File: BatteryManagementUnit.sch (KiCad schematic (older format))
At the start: 12 parts

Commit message: triac hack
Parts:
- removed U?: OPTO-TRANSISTOR, symbol OPTO-TRANSISTOR
- added Q?: Q_NPN_BCE, symbol Q_NPN_BCE
- added U?: OPTO-TRIAC, symbol OPTO-TRIAC
- P1: renamed from P?; footprint (none) -> Pin_Headers:Pin_Header_Angled_1x04
- P2, P3: renamed from P?; footprint (none) -> Pin_Headers:Pin_Header_Angled_1x02
- P4, P5: renamed from P?; footprint (none) -> Connect:bornier2
- Q1, Q2: renamed from Q?; footprint (none) -> TO_SOT_Packages_SMD:TO-252-2Lead
- R1, R2: renamed from R?; footprint (none) -> Resistors_SMD:R_1210_HandSoldering
- U2: renamed from U?; footprint (none) -> electric_car_lib:amc1301
- gave numbers to parts that had none: 1
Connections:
- wire segments 38 -> 39
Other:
- note removed: "CHOOSE HIGH VOLTAGE OPTO TRANSISTOR"

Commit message: partial layout
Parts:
- added P104: CONT_H_mon, Connect:bornier2, symbol CONN_01X02
- added P105: CONT_L_mon, Connect:bornier2, symbol CONN_01X02
- added P?: Battery, Connect:bornier2, symbol CONN_01X02
- Q101: renamed from Q?; footprint (none) -> TO_SOT_Packages_SMD:SOT-23_Handsoldering
- gave numbers to parts that had none: 1
- renumbered P1 to P101, P2 to P102, P3 to P103, P4 to P106, P5 to P107, Q1 to Q102, Q2 to Q103, R1 to R101, R2 to R102, U2 to U102, U3 to U103
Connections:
- wire segments 39 -> 47
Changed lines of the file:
@@
 $Descr A4 11693 8268
 encoding utf-8
-Sheet 1 1
+Sheet 1 2
 Title ""
 Date ""
@@
 $EndDescr
 $Comp
-L CONN_01X04 P1
+L CONN_01X04 P101
 U 1 1 57FC851F
 P 2800 1300
-F 0 "P1" H 2800 1550 50  0000 C CNN
+F 0 "P101" H 2800 1550 50  0000 C CNN
 F 1 "HALL EFFECT" V 2900 1300 50  0000 C CNN
 F 2 "Pin_Headers:Pin_Header_Angled_1x04" H 2800 1300 50  0001 C CNN
@@
 $EndComp
 $Comp
-L AMC1301 U2
+L AMC1301 U102
 U 1 1 57FC8658
 P 2400 6650
-F 0 "U2" H 2400 6300 60  0000 C CNN
+F 0 "U102" H 2400 6300 60  0000 C CNN
 F 1 "AMC1301" H 2400 7000 60  0000 C CNN
 F 2 "electric_car_lib:amc1301" H 2450 6200 60  0001 C CNN
@@
 $EndComp
 $Comp
-L R R1
+L R R101
 U 1 1 57FC8843
 P 1050 5200
-F 0 "R1" V 1130 5200 50  0000 C CNN
+F 0 "R101" V 1130 5200 50  0000 C CNN
 F 1 "R" V 1050 5200 50  0000 C CNN
 F 2 "Resistors_SMD:R_1210_HandSoldering" V 980 5200 50  0001 C CNN
@@
 $EndComp
 $Comp
-L R R2
+L R R102
 U 1 1 57FC8882
 P 1050 6050
-F 0 "R2" V 1130 6050 50  0000 C CNN
+F 0 "R102" V 1130 6050 50  0000 C CNN
 F 1 "R" V 1050 6050 50  0000 C CNN
 F 2 "Resistors_SMD:R_1210_HandSoldering" V 980 6050 50  0001 C CNN
@@
 $EndComp
 $Comp
-L Q_NMOS_DGS Q1
+L Q_NMOS_DGS Q102
 U 1 1 57FCE6EE
 P 8700 1550
-F 0 "Q1" H 9000 1600 50  0000 R CNN
+F 0 "Q102" H 9000 1600 50  0000 R CNN
 F 1 "Q_NMOS_DGS" H 9350 1500 50  0000 R CNN
 F 2 "TO_SOT_Packages_SMD:TO-252-2Lead" H 8900 1650 50  0001 C CNN
@@
 $EndComp
 $Comp
-L Teensy_3.2 U3
+L Teensy_3.2 U103
 U 1 1 57FCF1AF
 P 9500 4700
-F 0 "U3" H 9500 4550 39  0000 C CNN
+F 0 "U103" H 9500 4550 39  0000 C CNN
 F 1 "Teensy_3.2" H 9500 5250 39  0000 C CNN
 F 2 "" H 9200 4250 39  0001 C CNN
@@
 	1    0    0    -1
 $EndComp
-Text Label 1550 4500 1    60   ~ 0
+Text Label 850  4600 1    60   ~ 0
 HV+
 Text Label 1000 6650 1    60   ~ 0
@@
 out
 $Comp
-L CONN_01X02 P4
+L CONN_01X02 P106
 U 1 1 57FD399B
 P 8650 950
-F 0 "P4" H 8650 1100 50  0000 C CNN
+F 0 "P106" H 8650 1100 50  0000 C CNN
 F 1 "CONT_H" V 8750 950 50  0000 C CNN
 F 2 "Connect:bornier2" H 8650 950 50  0001 C CNN
@@
 CNT_H
 $Comp
-L Q_NMOS_DGS Q2
+L Q_NMOS_DGS Q103
 U 1 1 57FD434A
 P 10000 1550
-F 0 "Q2" H 10300 1600 50  0000 R CNN
+F 0 "Q103" H 10300 1600 50  0000 R CNN
 F 1 "Q_NMOS_DGS" H 10650 1500 50  0000 R CNN
 F 2 "TO_SOT_Packages_SMD:TO-252-2Lead" H 10200 1650 50  0001 C CNN
@@
 $EndComp
 $Comp
-L CONN_01X02 P5
+L CONN_01X02 P107
 U 1 1 57FD4357
 P 9950 950
-F 0 "P5" H 9950 1100 50  0000 C CNN
+F 0 "P107" H 9950 1100 50  0000 C CNN
 F 1 "CONT_L" V 10050 950 50  0000 C CNN
 F 2 "Connect:bornier2" H 9950 950 50  0001 C CNN
@@
 cell monitor
 $Comp
-L CONN_01X02 P3
+L CONN_01X02 P103
 U 1 1 57FD4B7A
 P 5350 4150
-F 0 "P3" H 5350 4300 50  0000 C CNN
+F 0 "P103" H 5350 4300 50  0000 C CNN
 F 1 "CONN_01X02" V 5450 4150 50  0000 C CNN
 F 2 "Pin_Headers:Pin_Header_Angled_1x02" H 5350 4150 50  0001 C CNN
@@
 $EndComp
 $Comp
-L CONN_01X02 P2
+L CONN_01X02 P102
 U 1 1 57FD4C12
 P 5300 5000
-F 0 "P2" H 5300 5150 50  0000 C CNN
+F 0 "P102" H 5300 5150 50  0000 C CNN
 F 1 "CONN_01X02" V 5400 5000 50  0000 C CNN
 F 2 "Pin_Headers:Pin_Header_Angled_1x02" H 5300 5000 50  0001 C CNN
@@
 c_m_L
 $Comp
-L OPTO-TRIAC U?
+L OPTO-TRIAC U101
 U 1 1 580F364D
 P 2200 4550
-F 0 "U?" H 2000 4750 50  0000 L CNN
+F 0 "U101" H 2000 4750 50  0000 L CNN
 F 1 "OPTO-TRIAC" H 2000 4350 50  0000 L CNN
-F 2 "" H 2200 4550 50  0000 L CIN
+F 2 "" H 2200 4550 50  0001 L CIN
 F 3 "" H 2175 4550 50  0000 L CNN
 	1    2200 4550
@@
 $EndComp
 $Comp
-L Q_NPN_BCE Q?
+L Q_NPN_BCE Q101
 U 1 1 580F386C
 P 1700 4650
-F 0 "Q?" H 2000 4700 50  0000 R CNN
+F 0 "Q101" H 2000 4700 50  0000 R CNN
 F 1 "Q_NPN_BCE" H 2300 4600 50  0000 R CNN
-F 2 "" H 1900 4750 50  0000 C CNN
+F 2 "TO_SOT_Packages_SMD:SOT-23_Handsoldering" H 1900 4750 50  0001 C CNN
 F 3 "" H 1700 4650 50  0000 C CNN
 	1    1700 4650
@@
 Connection ~ 550  4100
 Wire Wire Line
-	1050 5350 1050 5900
+	1050 5350 1050 5600
+Wire Wire Line
+	1050 5600 1050 5900
 Wire Wire Line
 	1050 6200 1050 6800
@@
 Connection ~ 1050 5600
 Wire Wire Line
+	850  6800 1050 6800
+Wire Wire Line
 	1050 6800 1800 6800
 Wire Wire Line
@@
 	4500 3200 7600 3200
 Wire Notes Line
-	7600 3200 7600 6200
+	6550 3200 6550 6200
 Wire Wire Line
 	5550 4100 6150 4100
@@
 	8800 4700 8350 4700
 Wire Wire Line
-	1900 4450 1600 4450
+	850  4450 1600 4450
+Wire Wire Line
+	1600 4450 1900 4450
 Wire Wire Line
 	1600 4850 1050 4850
 Wire Wire Line
-	1050 4800 1050 5050
-Connection ~ 1050 4800
+	1050 4850 1050 4850
+Wire Wire Line
+	1050 4850 1050 5050
+$Comp
+L CONN_01X02 P104
+U 1 1 582A7B5F
+P 5550 1000
+F 0 "P104" H 5550 1150 50  0000 C CNN
+F 1 "CONT_H_mon" V 5650 1000 50  0000 C CNN
+F 2 "Connect:bornier2" H 5550 1000 50  0001 C CNN
+F 3 "" H 5550 1000 50  0000 C CNN
+	1    5550 1000
+	0    -1   -1   0
+$EndComp
+$Comp
+L CONN_01X02 P105
+U 1 1 582A7BD5
+P 6150 1000
+F 0 "P105" H 6150 1150 50  0000 C CNN
+F 1 "CONT_L_mon" V 6250 1000 50  0000 C CNN
+F 2 "Connect:bornier2" H 6150 1000 50  0001 C CNN
+F 3 "" H 6150 1000 50  0000 C CNN
+	1    6150 1000
+	0    -1   -1   0
+$EndComp
+$Sheet
+S 6850 4100 1100 1000
+U 582A80B4
+F0 "CANmodule" 60
+F1 "CANmodule.sch" 60
+F2 "CAN_TX" I R 7950 4400 60
+F3 "CAN_RX" I R 7950 4500 60
+$EndSheet
+Wire Wire Line
+	8800 4400 7950 4400
+Wire Wire Line
+	7950 4500 8800 4500
+$Comp
+L CONN_01X02 P?
+U 1 1 582AAD74
+P 650 4700
+F 0 "P?" H 650 4850 50  0000 C CNN
+F 1 "Battery" V 750 4700 50  0000 C CNN
+F 2 "Connect:bornier2" H 650 4700 50  0001 C CNN
+F 3 "" H 650 4700 50  0000 C CNN
+	1    650  4700
+	-1   0    0    -1
+$EndComp
+Wire Wire Line
+	850  4650 850  4450
+Connection ~ 1600 4450
+Wire Wire Line
+	850  4750 850  6800
+Connection ~ 1050 6800
+Text Label 850  5050 1    60   ~ 0
+HV-
 $EndSCHEMATC

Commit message: completed schematic
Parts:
- added J101: 0, Resistors_SMD:R_1210_HandSoldering, symbol R
- added P109: PSU_ISO_3v, Pin_Headers:Pin_Header_Straight_1x04, symbol CONN_01X04
- added P110: PSU_ISO_5v, Pin_Headers:Pin_Header_Straight_1x04, symbol CONN_01X04
- added Q104, Q105: Q_NPN_BCE, TO_SOT_Packages_SMD:SOT-23_Handsoldering, symbol Q_NPN_BCE
- added R103, R104, R108, R109: 1k, Resistors_SMD:R_1210_HandSoldering, symbol R
- added R105: 10k 2W, Resistors_ThroughHole:Resistor_Cement_KOA-BGR-3N, symbol R
- added R106, R107, R111: 120, Resistors_SMD:R_1210_HandSoldering, symbol R
- added R110: 10K 2W, Resistors_ThroughHole:Resistor_Cement_KOA-BGR-3N, symbol R
- added R112, R113: 33, Resistors_SMD:R_1210_HandSoldering, symbol R
- added U104, U108: TLP2361, electric_car_lib:soic-5, symbol TLP2361
- added U105, U109: OPTO-TRIAC, symbol OPTO-TRIAC
- added U106: AP1117D33, TO_SOT_Packages_SMD:TO-263-3Lead, symbol AP1117D33
- added U107: AP1117E50, TO_SOT_Packages_SMD:TO-263-3Lead, symbol AP1117E50
- P101: footprint Pin_Headers:Pin_Header_Angled_1x04 -> Pin_Headers:Pin_Header_Straight_1x04
- P102: value CONN_01X02 -> cellsL; footprint Pin_Headers:Pin_Header_Angled_1x02 -> Pin_Headers:Pin_Header_Straight_1x02
- P103: value CONN_01X02 -> cellsH; footprint Pin_Headers:Pin_Header_Angled_1x02 -> Pin_Headers:Pin_Header_Straight_1x02
- U103: footprint (none) -> electric_car_lib:Teensy3.2_inv
- gave numbers to parts that had none: 1
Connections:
- net labels added: +3V3, +5VA, 5v_Traction, Cont_rdy_H, Cont_rdy_L, GND, GNDA, GND_Traction, PrechargeH, PrechargeL
- net labels removed: c_m_H, c_m_L, ground, voltage5v
- wire segments 47 -> 117
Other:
- note removed: "3.3v"
- note removed: "5v"
- note removed: "out"
- moved on the sheet: P104, P105

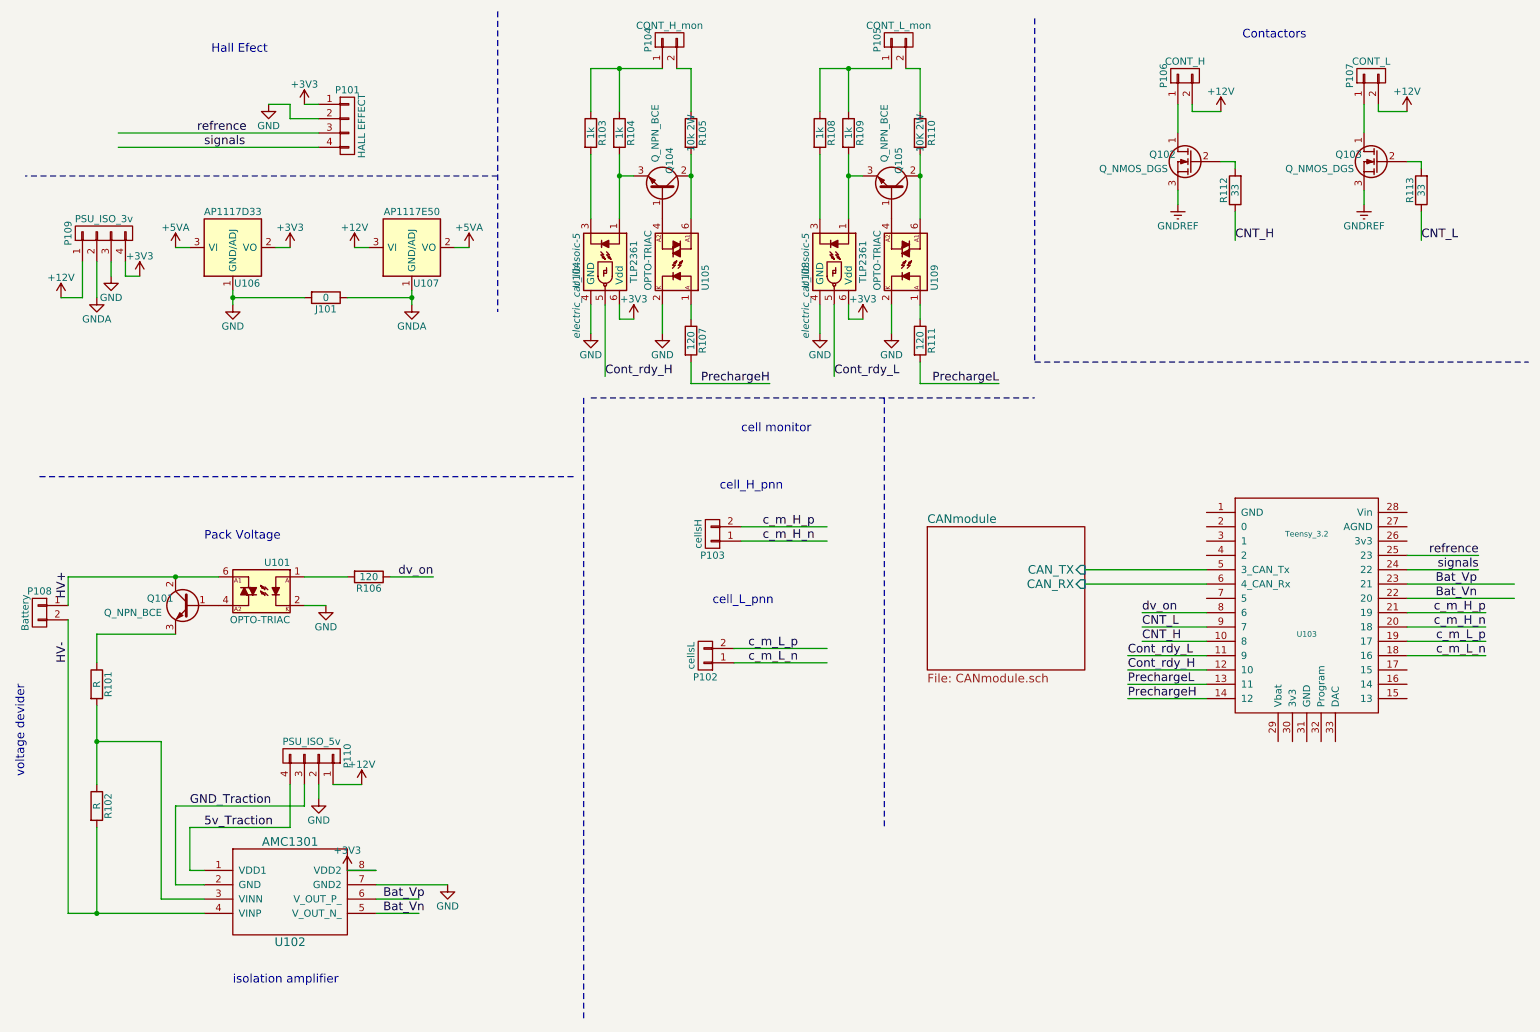
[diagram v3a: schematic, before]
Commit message: changed footprints, corrected psu, grouped parts
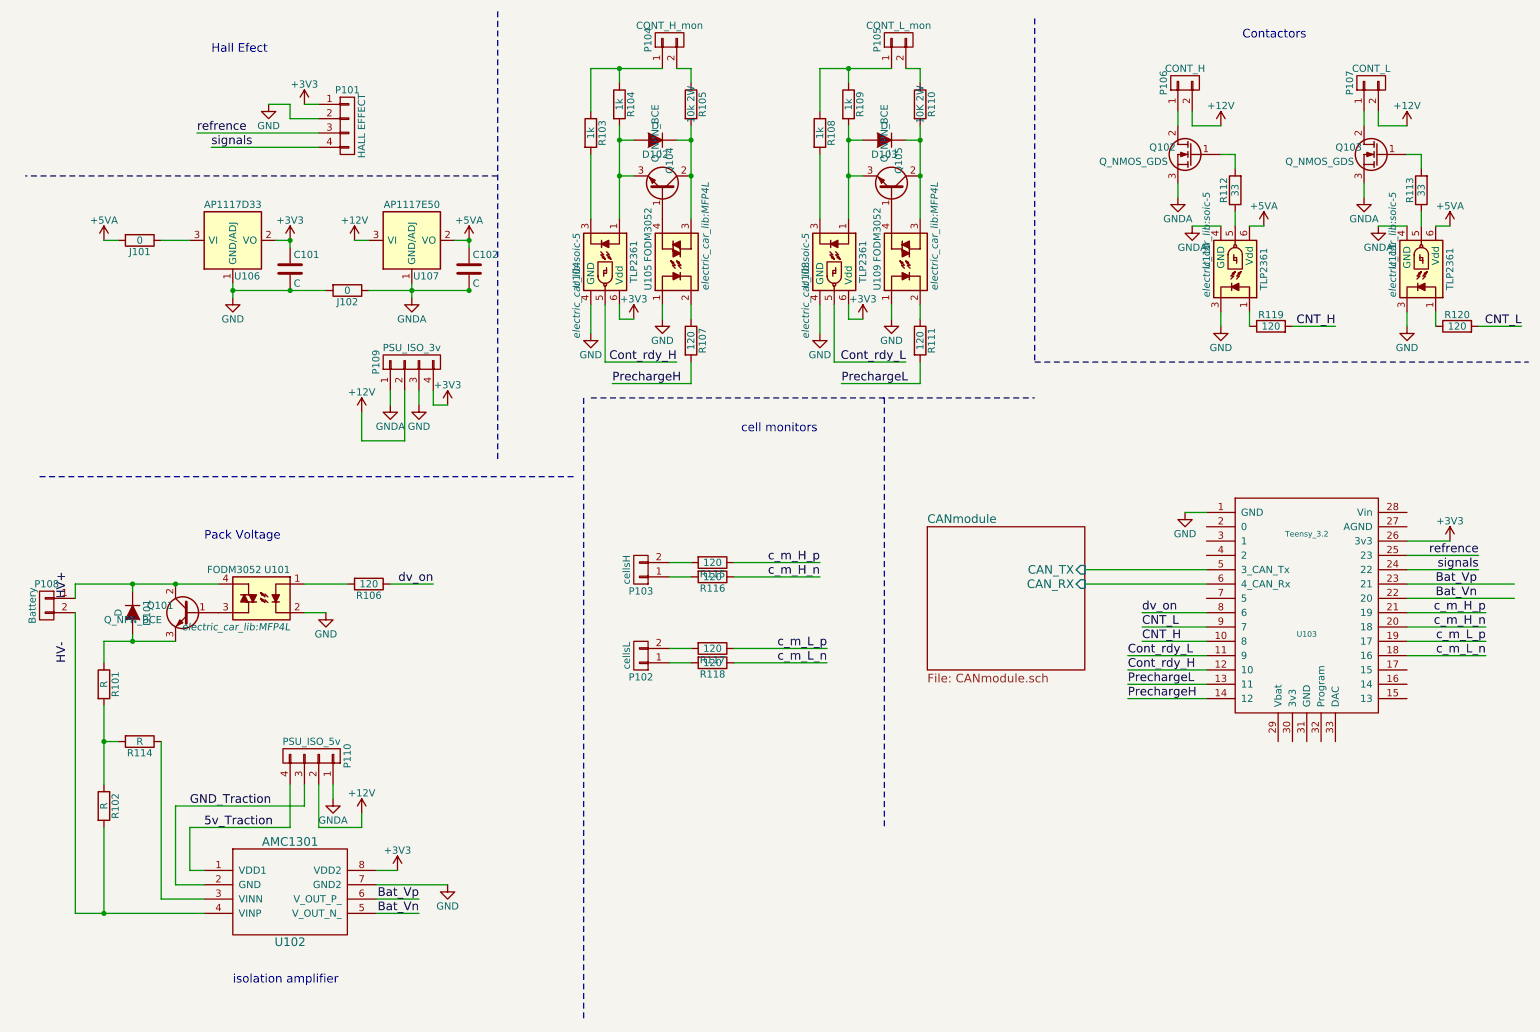
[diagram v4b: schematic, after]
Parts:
- removed Q102, Q103: Q_NMOS_DGS, TO_SOT_Packages_SMD:TO-252-2Lead, symbol Q_NMOS_DGS
- removed U101, U105, U109: OPTO-TRIAC, symbol OPTO-TRIAC
- added C101, C102: C, Capacitors_SMD:C_1210_HandSoldering, symbol C
- added D101, D102, D103: D, Diodes_SMD:DO-214AB_Handsoldering, symbol D
- added J102: 0, Resistors_SMD:R_1210_HandSoldering, symbol R
- added Q102, Q103: Q_NMOS_GDS, TO_SOT_Packages_SMD:TO-252-2Lead, symbol Q_NMOS_GDS
- added R114: R, Resistors_SMD:R_1206_HandSoldering, symbol R
- added R115, R116, R117, R118, R119, R120: 120, Resistors_SMD:R_1206_HandSoldering, symbol R
- added U101, U105, U109: FODM3052, electric_car_lib:MFP4L, symbol FODM3052
- added U110, U111: TLP2361, electric_car_lib:soic-5, symbol TLP2361
- Q101, Q104, Q105: footprint TO_SOT_Packages_SMD:SOT-23_Handsoldering -> TO_SOT_Packages_SMD:TO-252-2Lead
- R101, R102, R103, R104, R106, R107, R108, R109, R111, R112, R113: footprint Resistors_SMD:R_1210_HandSoldering -> Resistors_SMD:R_1206_HandSoldering
- U103: footprint electric_car_lib:Teensy3.2_inv -> electric_car_lib:Teensy3.2
- U106, U107: footprint TO_SOT_Packages_SMD:TO-263-3Lead -> TO_SOT_Packages_SMD:SOT-223
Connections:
- net labels removed: GNDREF
- wire segments 117 -> 147
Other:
- note added: "cell monitors"
- note removed: "cell monitor"
- note removed: "cell_H_pnn"
- note removed: "cell_L_pnn"
- note removed: "voltage devider"
- moved on the sheet: J101, P102, P103, P106, P107, P108, P109, Q101, R101, R102, R104, R105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
